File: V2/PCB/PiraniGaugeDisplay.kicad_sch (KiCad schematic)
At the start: 75 parts, among them J101 AuxIN, J102 Conn_02x03_Odd_Even, J103 RJ45, U101 AMS1117-3.3, U102 SN75176AD, U103 LM2596S-5, U104 ESP32-S3-WROOM-1(N16R2), U105 SW-SMD_L6.1-W3.5-LS8.0, U106 SW-SMD_L6.1-W3.5-LS8.0

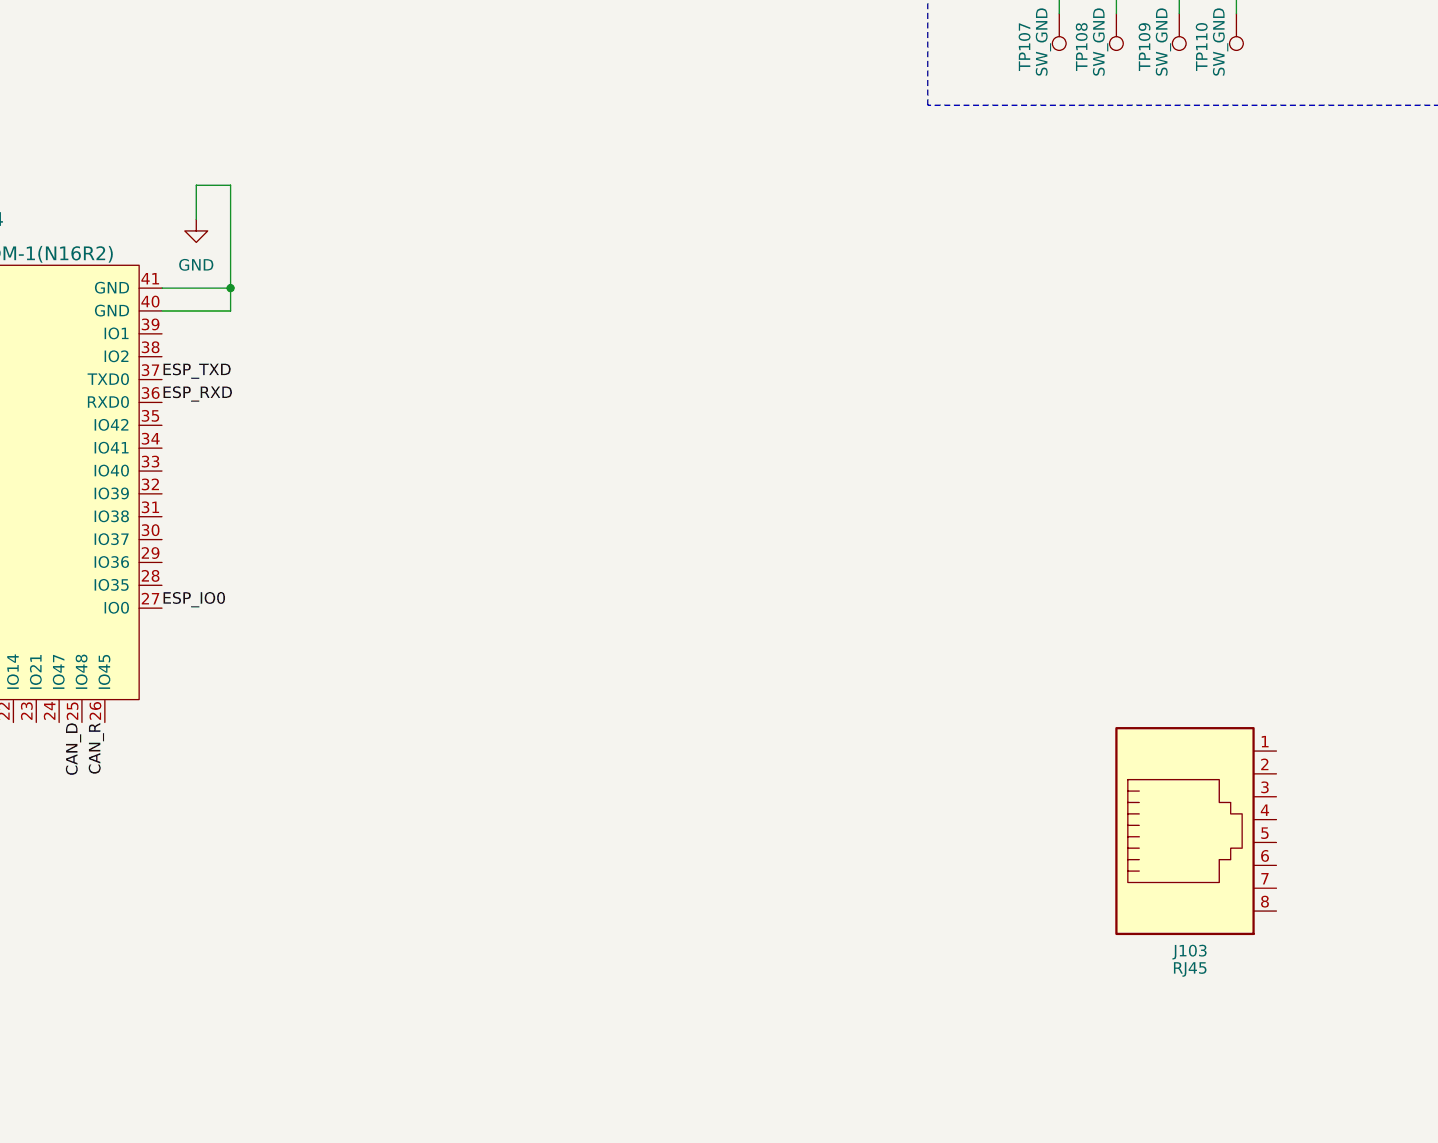
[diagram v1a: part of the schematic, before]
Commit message: Added ADC
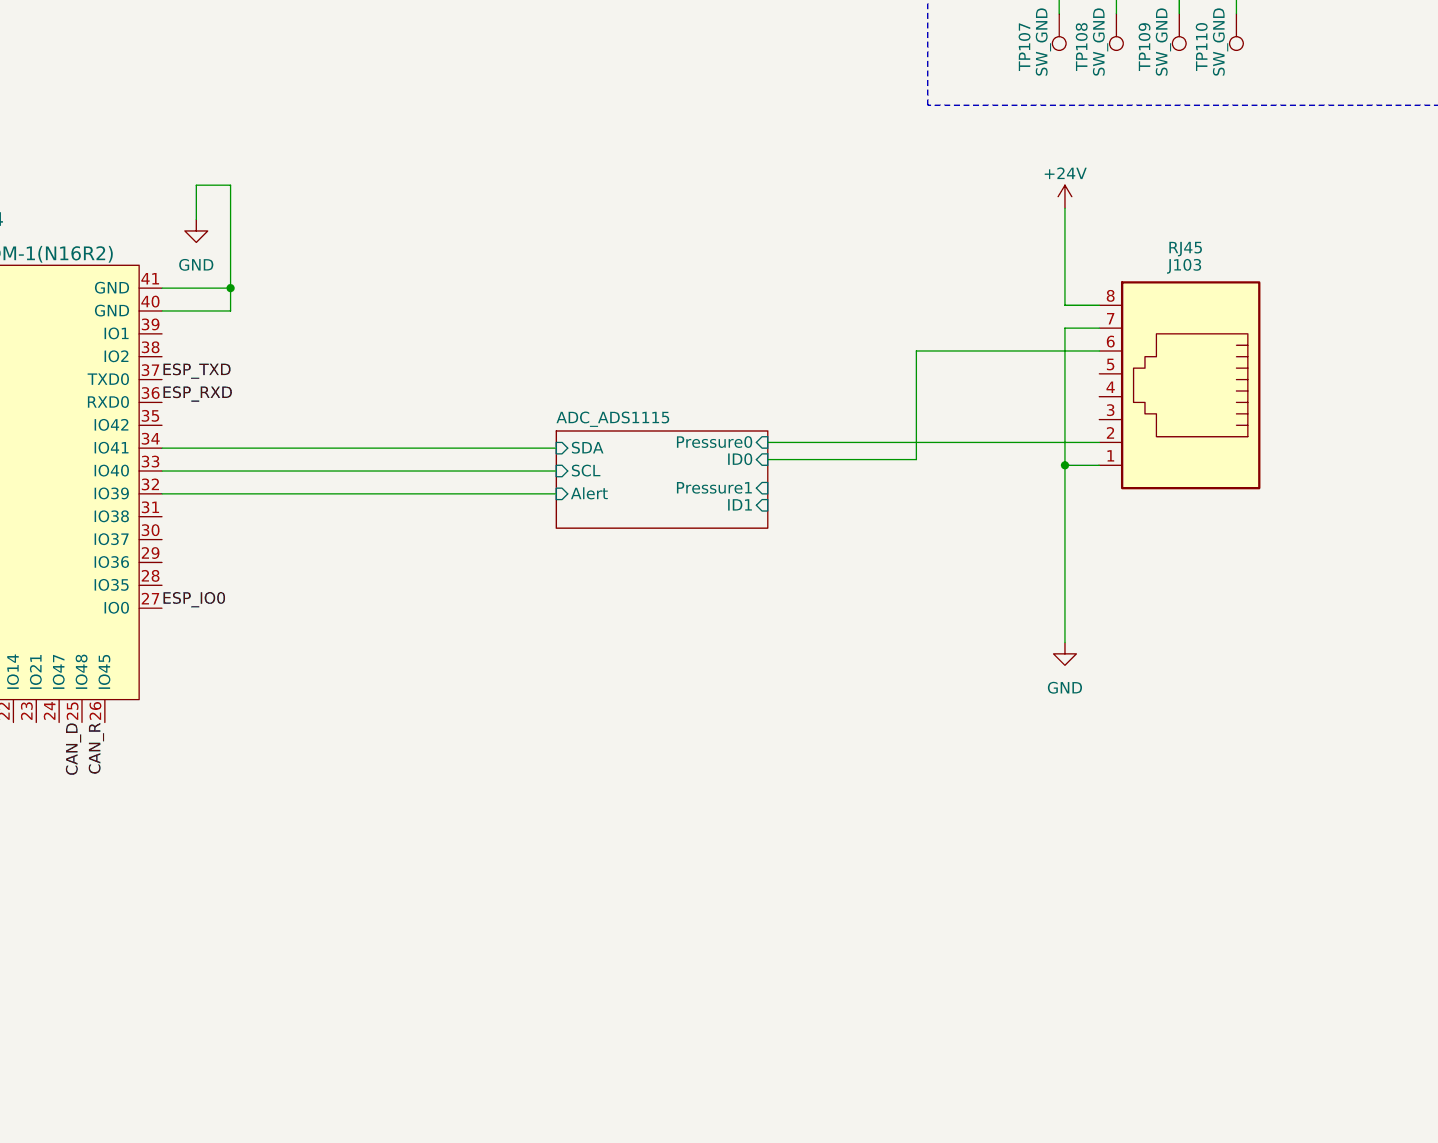
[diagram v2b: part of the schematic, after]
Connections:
- net +24V: now also J103.8
- net GND: now also J103.1, J103.7
- net ADC_ADS1115/Pressure0: now reaches J103.2
- net ADC_ADS1115/ID0: now reaches J103.6
- net ADC_ADS1115/Alert: now reaches U104.32 (IO39)
- net ADC_ADS1115/SCL: now reaches U104.33 (IO40)
- net ADC_ADS1115/SDA: now reaches U104.34 (IO41)
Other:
- added sheet ADC_ADS1115 (ADC_ADS1115.kicad_sch)
- moved on the sheet: J103
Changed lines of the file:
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@@
   (junction (at 111.76 153.67) (diameter 0) (color 0 0 0 0)
   )
+  (junction (at 285.75 168.275) (diameter 0) (color 0 0 0 0)
+  )
   (junction (at 283.21 35.56) (diameter 0) (color 0 0 0 0)
   )
@@
     (stroke (width 0) (type default))
   )
+  (wire (pts (xy 269.24 167.64) (xy 269.24 155.575))
+    (stroke (width 0) (type default))
+  )
   (wire (pts (xy 381.635 224.155) (xy 384.81 224.155))
     (stroke (width 0) (type default))
   )
+  (wire (pts (xy 289.56 150.495) (xy 285.75 150.495))
+    (stroke (width 0) (type default))
+  )
   (wire (pts (xy 360.045 92.71) (xy 360.045 90.805))
     (stroke (width 0) (type default))
@@
     (stroke (width 0) (type default))
   )
+  (wire (pts (xy 285.75 168.275) (xy 285.75 187.96))
+    (stroke (width 0) (type default))
+  )
   (wire (pts (xy 241.935 55.245) (xy 248.285 55.245))
     (stroke (width 0) (type default))
@@
     (stroke (width 0) (type default))
   )
+  (wire (pts (xy 269.24 155.575) (xy 289.56 155.575))
+    (stroke (width 0) (type default))
+  )
+  (wire (pts (xy 285.75 150.495) (xy 285.75 139.7))
+    (stroke (width 0) (type default))
+  )
   (wire (pts (xy 187.96 52.07) (xy 187.96 55.88))
     (stroke (width 0) (type default))
@@
     (stroke (width 0) (type default))
   )
+  (wire (pts (xy 289.56 153.035) (xy 285.75 153.035))
+    (stroke (width 0) (type default))
+  )
   (wire (pts (xy 371.475 105.41) (xy 371.475 113.03))
     (stroke (width 0) (type default))
@@
     (stroke (width 0) (type default))
   )
+  (wire (pts (xy 252.73 165.735) (xy 289.56 165.735))
+    (stroke (width 0) (type default))
+  )
   (wire (pts (xy 371.475 102.87) (xy 375.285 102.87))
     (stroke (width 0) (type default))
@@
     (stroke (width 0) (type default))
   )
+  (wire (pts (xy 185.42 166.37) (xy 229.235 166.37))
+    (stroke (width 0) (type default))
+  )
   (wire (pts (xy 140.97 139.065) (xy 140.97 148.59))
     (stroke (width 0) (type default))
@@
     (stroke (width 0) (type default))
   )
+  (wire (pts (xy 289.56 168.275) (xy 285.75 168.275))
+    (stroke (width 0) (type default))
+  )
+  (wire (pts (xy 185.42 171.45) (xy 229.235 171.45))
+    (stroke (width 0) (type default))
+  )
   (wire (pts (xy 290.83 89.535) (xy 290.83 95.885))
     (stroke (width 0) (type default))
@@
     (stroke (width 0) (type default))
   )
+  (wire (pts (xy 252.73 167.64) (xy 269.24 167.64))
+    (stroke (width 0) (type default))
+  )
   (wire (pts (xy 225.425 33.655) (xy 221.615 33.655))
     (stroke (width 0) (type default))
@@
     (stroke (width 0) (type default))
   )
+  (wire (pts (xy 185.42 168.91) (xy 229.235 168.91))
+    (stroke (width 0) (type default))
+  )
   (wire (pts (xy 225.425 37.465) (xy 225.425 38.735))
     (stroke (width 0) (type default))
@@
     (stroke (width 0) (type default))
   )
+  (wire (pts (xy 285.75 153.035) (xy 285.75 168.275))
+    (stroke (width 0) (type default))
+  )
   (wire (pts (xy 380.365 102.87) (xy 386.715 102.87))
     (stroke (width 0) (type default))
@@
     )
   )
-  (symbol (lib_id "PGD-Library:RJ45") (at 299.085 207.645 0) (mirror x) (unit 1)
+  (symbol (lib_id "PGD-Library:RJ45") (at 299.72 160.655 0) (mirror y) (unit 1)
     (in_bom yes) (on_board yes) (dnp no)
-    (property "Reference" "J103" (at 301.625 222.25 0)
+    (property "Reference" "J103" (at 297.18 146.05 0)
       (effects (font (size 1.27 1.27)) (justify right))
     )
-    (property "Value" "RJ45" (at 301.625 224.171 0)
+    (property "Value" "RJ45" (at 297.18 144.129 0)
       (effects (font (size 1.27 1.27)) (justify right))
     )
-    (property "Footprint" "SamacSys_Parts:55551621" (at 299.085 208.28 90)
+    (property "Footprint" "SamacSys_Parts:55551621" (at 299.72 160.02 90)
       (effects (font (size 1.27 1.27)) hide)
     )
-    (property "Datasheet" "https://jlcpcb.com/partdetail/TeConnectivity-55551621/C305976" (at 299.085 208.28 90)
+    (property "Datasheet" "https://jlcpcb.com/partdetail/TeConnectivity-55551621/C305976" (at 299.72 160.02 90)
       (effects (font (size 1.27 1.27)) hide)
     )
-    (property "MPN" "5555162-1" (at 299.085 207.645 0)
+    (property "MPN" "5555162-1" (at 299.72 160.655 0)
       (effects (font (size 1.27 1.27)) hide)
     )
-    (property "LCSC Part" "C305976" (at 299.085 207.645 0)
+    (property "LCSC Part" "C305976" (at 299.72 160.655 0)
       (effects (font (size 1.27 1.27)) hide)
     )
-    (property "JLC Part" "Extended Part" (at 299.085 207.645 0)
+    (property "JLC Part" "Extended Part" (at 299.72 160.655 0)
       (effects (font (size 1.27 1.27)) hide)
     )
@@
     )
   )
+  (symbol (lib_id "power:+24V") (at 285.75 139.7 0) (unit 1)
+    (in_bom yes) (on_board yes) (dnp no) (fields_autoplaced)
+    (property "Reference" "#PWR0159" (at 285.75 143.51 0)
+      (effects (font (size 1.27 1.27)) hide)
+    )
+    (property "Value" "+24V" (at 285.75 135.89 0)
+      (effects (font (size 1.27 1.27)))
+    )
+    (property "Footprint" "" (at 285.75 139.7 0)
+      (effects (font (size 1.27 1.27)) hide)
+    )
+    (property "Datasheet" "" (at 285.75 139.7 0)
+      (effects (font (size 1.27 1.27)) hide)
+    )
+    (pin "1")
+    (instances
+      (project "PiraniGaugeDisplay"
+        (path "/43dd4952-cc68-4687-8eb3-b9ec0d7c6e3f"
+          (reference "#PWR0159") (unit 1)
+        )
+      )
+      (project "Bincorp_485JoystickControllerV1"
+        (path "/5397a52a-2c54-44b7-9db3-8e4625eee83c"
+          (reference "#PWR0104") (unit 1)
+        )
+      )
+      (project "CAN-CalibratedTempProbeV1R1"
+        (path "/92e71201-b3e0-49fb-9b7c-0afb28a8eb71"
+          (reference "#PWR0106") (unit 1)
+        )
+      )
+    )
+  )
   (symbol (lib_id "power:GND") (at 364.49 229.87 0) (unit 1)
     (in_bom yes) (on_board yes) (dnp no)
@@
     )
   )
+  (symbol (lib_id "power:GND") (at 285.75 187.96 0) (unit 1)
+    (in_bom yes) (on_board yes) (dnp no) (fields_autoplaced)
+    (property "Reference" "#PWR0158" (at 285.75 194.31 0)
+      (effects (font (size 1.27 1.27)) hide)
+    )
+    (property "Value" "GND" (at 285.75 193.04 0)
+      (effects (font (size 1.27 1.27)))
+    )
+    (property "Footprint" "" (at 285.75 187.96 0)
+      (effects (font (size 1.27 1.27)) hide)
+    )
+    (property "Datasheet" "" (at 285.75 187.96 0)
+      (effects (font (size 1.27 1.27)) hide)
+    )
+    (pin "1")
+    (instances
+      (project "PiraniGaugeDisplay"
+        (path "/43dd4952-cc68-4687-8eb3-b9ec0d7c6e3f"
+          (reference "#PWR0158") (unit 1)
+        )
+      )
+      (project "Output_6Ch_SoftLimits"
+        (path "/4b0f5b1c-07df-47c2-aaba-21ba49ee7833/78e202ab-5c8d-4773-a7da-d36ce95b1f98"
+          (reference "#PWR0216") (unit 1)
+        )
+      )
+      (project "Bincorp_485JoystickControllerV1"
+        (path "/5397a52a-2c54-44b7-9db3-8e4625eee83c"
+          (reference "#PWR0132") (unit 1)
+        )
+      )
+      (project "Output_2ch_FaultTolerant"
+        (path "/822dc713-1e34-416c-8054-f7a476bb7106/af209f49-7f24-4fa8-ab98-ee0418753dcc"
+          (reference "#PWR035") (unit 1)
+        )
+      )
+    )
+  )
   (symbol (lib_id "power:GND") (at 168.91 50.8 0) (unit 1)
     (in_bom yes) (on_board yes) (dnp no) (fields_autoplaced)
@@
       )
     )
+  )
+  (sheet (at 229.235 164.465) (size 23.495 10.795) (fields_autoplaced)
+    (stroke (width 0.1524) (type solid))
+    (fill (color 0 0 0 0.0000))
+    (property "Sheetname" "ADC_ADS1115" (at 229.235 163.7534 0)
+      (effects (font (size 1.27 1.27)) (justify left bottom))
+    )
+    (property "Sheetfile" "ADC_ADS1115.kicad_sch" (at 229.235 175.8446 0)
+      (effects (font (size 1.27 1.27)) (justify left top) hide)
+    )
+    (pin "SDA" input (at 229.235 166.37 180)
+      (effects (font (size 1.27 1.27)) (justify left))
+    )
+    (pin "Alert" input (at 229.235 171.45 180)
+      (effects (font (size 1.27 1.27)) (justify left))
+    )
+    (pin "SCL" input (at 229.235 168.91 180)
+      (effects (font (size 1.27 1.27)) (justify left))
+    )
+    (pin "ID1" input (at 252.73 172.72 0)
+      (effects (font (size 1.27 1.27)) (justify right))
+    )
+    (pin "Pressure1" input (at 252.73 170.815 0)
+      (effects (font (size 1.27 1.27)) (justify right))
+    )
+    (pin "Pressure0" input (at 252.73 165.735 0)
+      (effects (font (size 1.27 1.27)) (justify right))
+    )
+    (pin "ID0" input (at 252.73 167.64 0)
+      (effects (font (size 1.27 1.27)) (justify right))
+    )
+    (instances
+      (project "PiraniGaugeDisplay"
+        (path "/43dd4952-cc68-4687-8eb3-b9ec0d7c6e3f" (page "4"))
+      )
+    )

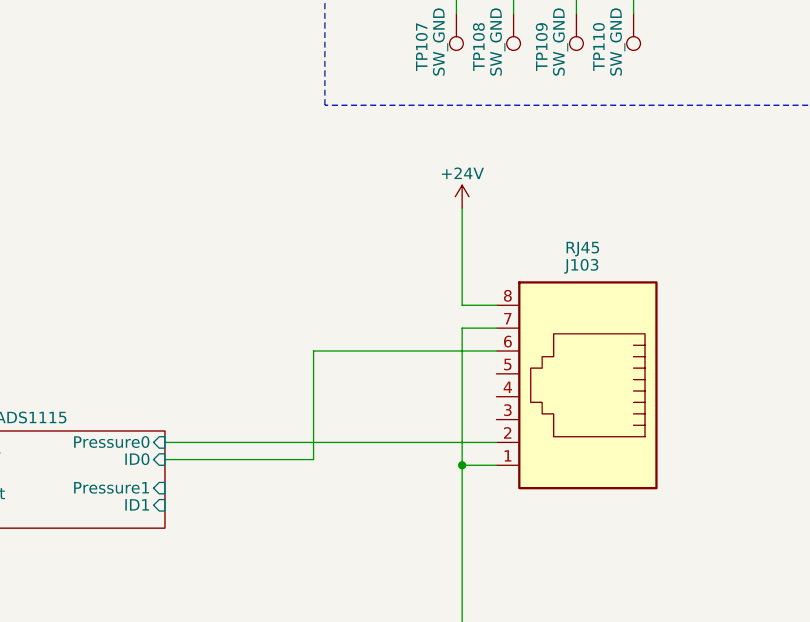
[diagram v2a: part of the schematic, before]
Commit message: Changed ADC divider
Changed ADC divider to give 1.9v for 10V in this matches up with the 2.048v input range on the ADC
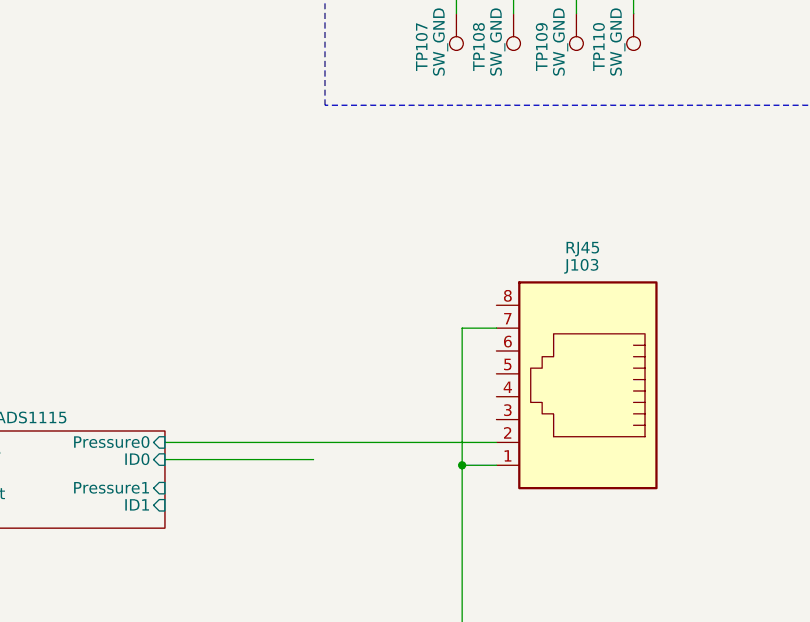
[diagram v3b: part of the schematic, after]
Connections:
- net +24V: no longer J103.8
- net ADC_ADS1115/ID0: no longer J103.6
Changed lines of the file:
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@@
-    (stroke (width 0) (type default))
-  )
-  (wire (pts (xy 269.24 167.64) (xy 269.24 155.575))
     (stroke (width 0) (type default))
   )
@@
     (stroke (width 0) (type default))
   )
-  (wire (pts (xy 289.56 150.495) (xy 285.75 150.495))
-    (stroke (width 0) (type default))
-  )
   (wire (pts (xy 360.045 92.71) (xy 360.045 90.805))
     (stroke (width 0) (type default))
@@
   )
   (wire (pts (xy 187.96 39.37) (xy 187.96 44.45))
-    (stroke (width 0) (type default))
-  )
-  (wire (pts (xy 269.24 155.575) (xy 289.56 155.575))
-    (stroke (width 0) (type default))
-  )
-  (wire (pts (xy 285.75 150.495) (xy 285.75 139.7))
     (stroke (width 0) (type default))
   )
@@
         )
       )
-      (project "Bincorp_485JoystickControllerV1"
-        (path "/5397a52a-2c54-44b7-9db3-8e4625eee83c"
-          (reference "#PWR0104") (unit 1)
-        )
-      )
-      (project "CAN-CalibratedTempProbeV1R1"
-        (path "/92e71201-b3e0-49fb-9b7c-0afb28a8eb71"
-          (reference "#PWR0106") (unit 1)
-        )
-      )
-    )
-  )
-  (symbol (lib_id "power:+24V") (at 285.75 139.7 0) (unit 1)
-    (in_bom yes) (on_board yes) (dnp no) (fields_autoplaced)
-    (property "Reference" "#PWR0159" (at 285.75 143.51 0)
-      (effects (font (size 1.27 1.27)) hide)
-    )
-    (property "Value" "+24V" (at 285.75 135.89 0)
-      (effects (font (size 1.27 1.27)))
-    )
-    (property "Footprint" "" (at 285.75 139.7 0)
-      (effects (font (size 1.27 1.27)) hide)
-    )
-    (property "Datasheet" "" (at 285.75 139.7 0)
-      (effects (font (size 1.27 1.27)) hide)
-    )
-    (pin "1")
-    (instances
-      (project "PiraniGaugeDisplay"
-        (path "/43dd4952-cc68-4687-8eb3-b9ec0d7c6e3f"
-          (reference "#PWR0159") (unit 1)
-        )
-      )
